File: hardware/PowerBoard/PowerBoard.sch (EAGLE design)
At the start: 136 parts, among them J1 CON-HRS-DM3AT, J2 CON-ZX62R-B-5P, J3 CON-FTSH-105-01-L-DV-K, J4 CON-S2B-PH-SM4-TB, J5 CON-PJ-102A, J6 CON-71741-0002-TOP, M1 MOUNT-HOLE3.3, M2 MOUNT-HOLE3.3, M3 MOUNT-HOLE3.3, M4 MOUNT-HOLE3.3, M5 FIDUCIAL1X2, M6 FIDUCIAL1X2, M7 FIDUCIAL1X2, M8 FIDUCIAL1X2, Q1 SI2323CDS, Q2 SI2312CDS, Q3 SI2333CDS, Q4 SI2333CDS, SW1 SWITCH-SPST, SW2 SWITCH-MS12ASG30, SW3 SWITCH-KSC-201J, U1 LTC4361-2DC, U10 MAX9938FEUK, U11 MAX9938FEUK, U12 MAX9938FEUK, U13 STM32F10XCXT6, U14 LTC2942-1, U15 USBLC6-2, U2 LTC4085, U3 XC6220B331MR-G, U4 XC6220B331MR-G, U5 XC9236A15DMR-G, U6 MIC94043, U8 MAX9938FEUK, U9 MAX9938FEUK, X1 ECX-2236, X2 ECX-31B

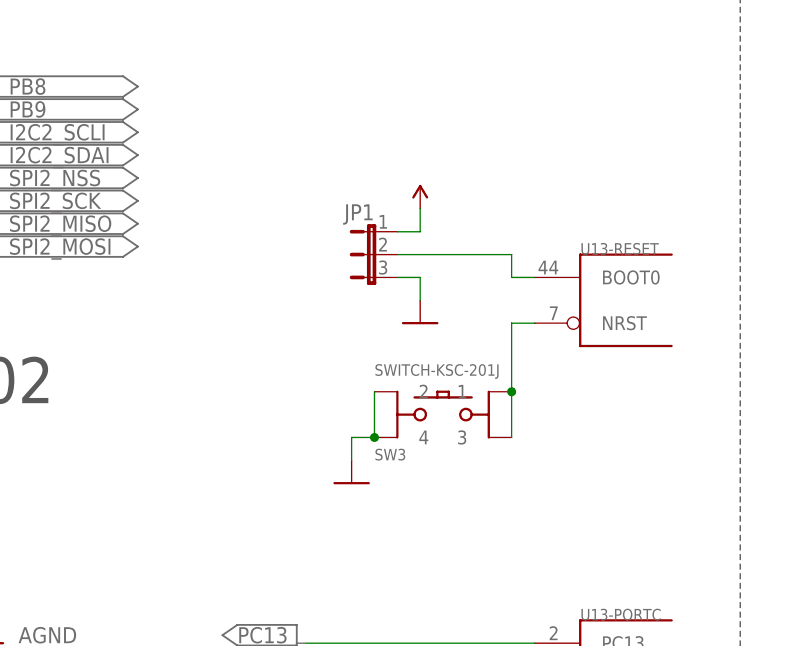
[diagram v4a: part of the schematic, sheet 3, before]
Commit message: - 90 degree push button for reset - Switch selectable boot - Some grounding
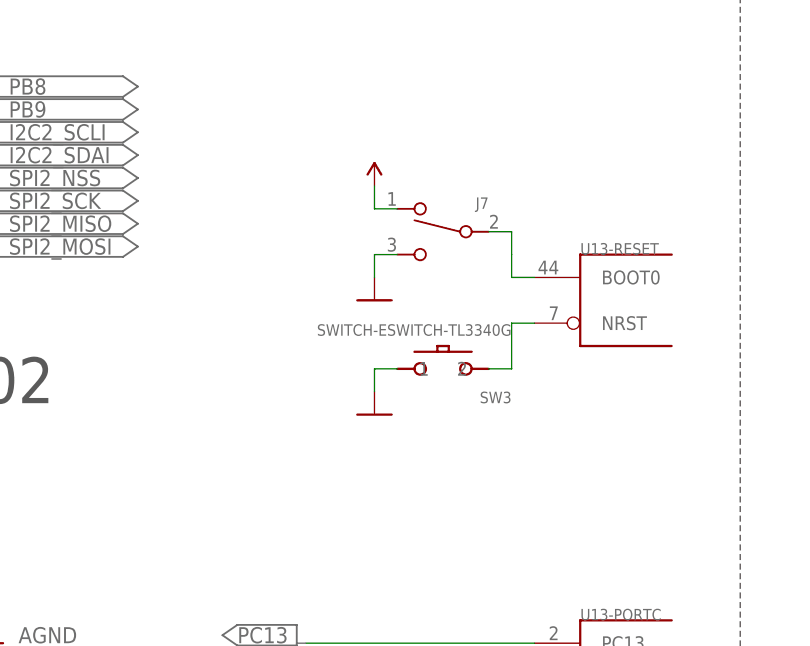
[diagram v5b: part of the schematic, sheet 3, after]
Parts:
- removed JP1: JUMPER-3PTH, powerboard:JUMPER-3PTH
- added J7: SWITCH-CJS-1200-1200, powerboard:SWITCH-CJS-1200-1200
- SW3: value SWITCH-KSC-201J -> SWITCH-ESWITCH-TL3340G; device powerboard:SWITCH-KSC-201J -> powerboard:SWITCH-ESWITCH-TL3340G
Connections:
- net BOOT0: now also J7.2; no longer JP1.2
- net D3V3_STM: now also J7.1; no longer JP1.1
- net DGND: now also J7.3, SW3.1; no longer JP1.3, SW3.2, SW3.4
- net NRST: now also SW3.2; no longer SW3.1, SW3.3
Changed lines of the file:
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@@
 <part name="PORT51" library="powerboard" deviceset="PORT7" device=""/>
 <part name="PORT52" library="powerboard" deviceset="PORT7" device=""/>
-<part name="JP1" library="powerboard" deviceset="JUMPER-3" device="PTH"/>
 <part name="U$42" library="powerboard" deviceset="D3V3_STM" device=""/>
 <part name="U$48" library="powerboard" deviceset="D3V3_STM" device=""/>
@@
 </part>
 <part name="PORT18" library="powerboard" deviceset="PORT7" device=""/>
-<part name="SW3" library="powerboard" deviceset="SWITCH-KSC" device="J" technology="-201"/>
 <part name="U$15" library="powerboard" deviceset="DGND" device=""/>
 <part name="PORT2" library="powerboard" deviceset="PORT7" device=""/>
@@
 <attribute name="TOLERANCE" value=""/>
 </part>
+<part name="SW3" library="powerboard" deviceset="SWITCH-ESWITCH-TL3340" device="G"/>
+<part name="J7" library="powerboard" deviceset="SWITCH-CJS-1200" device="-1200"/>
 </parts>
 <sheets>
@@
 <instance part="PORT51" gate="G$1" x="170.18" y="134.62"/>
 <instance part="PORT52" gate="G$1" x="170.18" y="132.08"/>
-<instance part="JP1" gate="G$1" x="198.12" y="119.38" smashed="yes" rot="MR270">
-<attribute name="NAME" x="198.12" y="120.65" size="1.778" layer="95" rot="MR0"/>
-</instance>
-<instance part="U$42" gate="G$1" x="203.2" y="121.92" smashed="yes" rot="MR0"/>
+<instance part="U$42" gate="G$1" x="198.12" y="124.46" smashed="yes" rot="MR0"/>
 <instance part="U$48" gate="G$1" x="154.94" y="88.9" rot="MR0"/>
 <instance part="LED1" gate="G$1" x="195.58" y="154.94"/>
@@
 <instance part="PORT58" gate="G$1" x="182.88" y="68.58" rot="MR0"/>
 <instance part="PORT59" gate="G$1" x="182.88" y="63.5" rot="MR0"/>
-<instance part="U$37" gate="G$1" x="203.2" y="109.22" rot="MR0"/>
+<instance part="U$37" gate="G$1" x="198.12" y="111.76" rot="MR0"/>
 <instance part="PORT60" gate="G$1" x="228.6" y="147.32"/>
 <instance part="PORT61" gate="G$1" x="91.44" y="17.78" rot="MR0"/>
@@
 </instance>
 <instance part="PORT18" gate="G$1" x="10.16" y="177.8" rot="MR0"/>
-<instance part="SW3" gate="G$1" x="205.74" y="99.06"/>
-<instance part="U$15" gate="G$1" x="195.58" y="91.44" rot="MR0"/>
+<instance part="U$15" gate="G$1" x="198.12" y="99.06" rot="MR0"/>
 <instance part="U$67" gate="G$1" x="40.64" y="152.4"/>
 <instance part="U$68" gate="G$1" x="27.94" y="124.46"/>
 <instance part="U$69" gate="G$1" x="27.94" y="96.52"/>
 <instance part="U$70" gate="G$1" x="27.94" y="68.58"/>
+<instance part="SW3" gate="G$1" x="205.74" y="104.14" rot="MR0"/>
+<instance part="J7" gate="G$1" x="205.74" y="119.38" rot="MR0"/>
 </instances>
 <busses>
@@
 </segment>
 <segment>
-<wire x1="200.66" y1="114.3" x2="203.2" y2="114.3" width="0.1524" layer="91"/>
-<pinref part="JP1" gate="G$1" pin="3"/>
 <pinref part="U$37" gate="G$1" pin="DGND"/>
-<wire x1="203.2" y1="114.3" x2="203.2" y2="111.76" width="0.1524" layer="91"/>
-</segment>
-<segment>
-<pinref part="SW3" gate="G$1" pin="2"/>
-<pinref part="SW3" gate="G$1" pin="4"/>
-<junction x="198.12" y="96.52"/>
-<wire x1="198.12" y1="101.6" x2="198.12" y2="96.52" width="0.1524" layer="91"/>
-<wire x1="198.12" y1="96.52" x2="195.58" y2="96.52" width="0.1524" layer="91"/>
+<wire x1="200.66" y1="116.84" x2="198.12" y2="116.84" width="0.1524" layer="91"/>
+<wire x1="198.12" y1="116.84" x2="198.12" y2="114.3" width="0.1524" layer="91"/>
+<pinref part="J7" gate="G$1" pin="3"/>
+</segment>
+<segment>
+<wire x1="198.12" y1="104.14" x2="198.12" y2="101.6" width="0.1524" layer="91"/>
 <pinref part="U$15" gate="G$1" pin="DGND"/>
-<wire x1="195.58" y1="96.52" x2="195.58" y2="93.98" width="0.1524" layer="91"/>
+<pinref part="SW3" gate="G$1" pin="1"/>
+<wire x1="198.12" y1="104.14" x2="200.66" y2="104.14" width="0.1524" layer="91"/>
 </segment>
 <segment>
@@
 </segment>
 <segment>
-<wire x1="200.66" y1="119.38" x2="203.2" y2="119.38" width="0.1524" layer="91"/>
-<wire x1="203.2" y1="119.38" x2="203.2" y2="121.92" width="0.1524" layer="91"/>
-<pinref part="JP1" gate="G$1" pin="1"/>
+<wire x1="200.66" y1="121.92" x2="198.12" y2="121.92" width="0.1524" layer="91"/>
+<wire x1="198.12" y1="121.92" x2="198.12" y2="124.46" width="0.1524" layer="91"/>
 <pinref part="U$42" gate="G$1" pin="D3V3_STM"/>
+<pinref part="J7" gate="G$1" pin="1"/>
 </segment>
 <segment>
@@
 <segment>
 <wire x1="215.9" y1="109.22" x2="213.36" y2="109.22" width="0.1524" layer="91"/>
-<wire x1="213.36" y1="109.22" x2="213.36" y2="101.6" width="0.1524" layer="91"/>
+<wire x1="213.36" y1="109.22" x2="213.36" y2="104.14" width="0.1524" layer="91"/>
 <pinref part="U13" gate="-RESET" pin="NRST"/>
-<pinref part="SW3" gate="G$1" pin="1"/>
-<wire x1="213.36" y1="101.6" x2="213.36" y2="96.52" width="0.1524" layer="91"/>
-<junction x="213.36" y="101.6"/>
-<pinref part="SW3" gate="G$1" pin="3"/>
+<pinref part="SW3" gate="G$1" pin="2"/>
+<wire x1="210.82" y1="104.14" x2="213.36" y2="104.14" width="0.1524" layer="91"/>
 </segment>
 </net>
@@
 <wire x1="215.9" y1="114.3" x2="213.36" y2="114.3" width="0.1524" layer="91"/>
 <wire x1="213.36" y1="114.3" x2="213.36" y2="116.84" width="0.1524" layer="91"/>
-<wire x1="213.36" y1="116.84" x2="200.66" y2="116.84" width="0.1524" layer="91"/>
+<wire x1="213.36" y1="116.84" x2="213.36" y2="119.38" width="0.1524" layer="91"/>
+<wire x1="213.36" y1="119.38" x2="210.82" y2="119.38" width="0.1524" layer="91"/>
 <pinref part="U13" gate="-RESET" pin="BOOT0"/>
-<pinref part="JP1" gate="G$1" pin="2"/>
-</segment>
-</net>
+<pinref part="J7" gate="G$1" pin="2"/>
+</segment>
+</net>
